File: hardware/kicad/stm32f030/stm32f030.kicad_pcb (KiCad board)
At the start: 2 copper layers, 67.3 x 69.2 mm, 114 parts, among them IC1 AT24CS02-SSHM, K1 RELAY_1RT, K2 RELAY_1RT, P1 5VIN, P10 SWD, P2 LOOP1, P3 LOOP2, P4 RELAY OUT 1, P5 TTL OUT 1, P6 RELAY OUT 2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

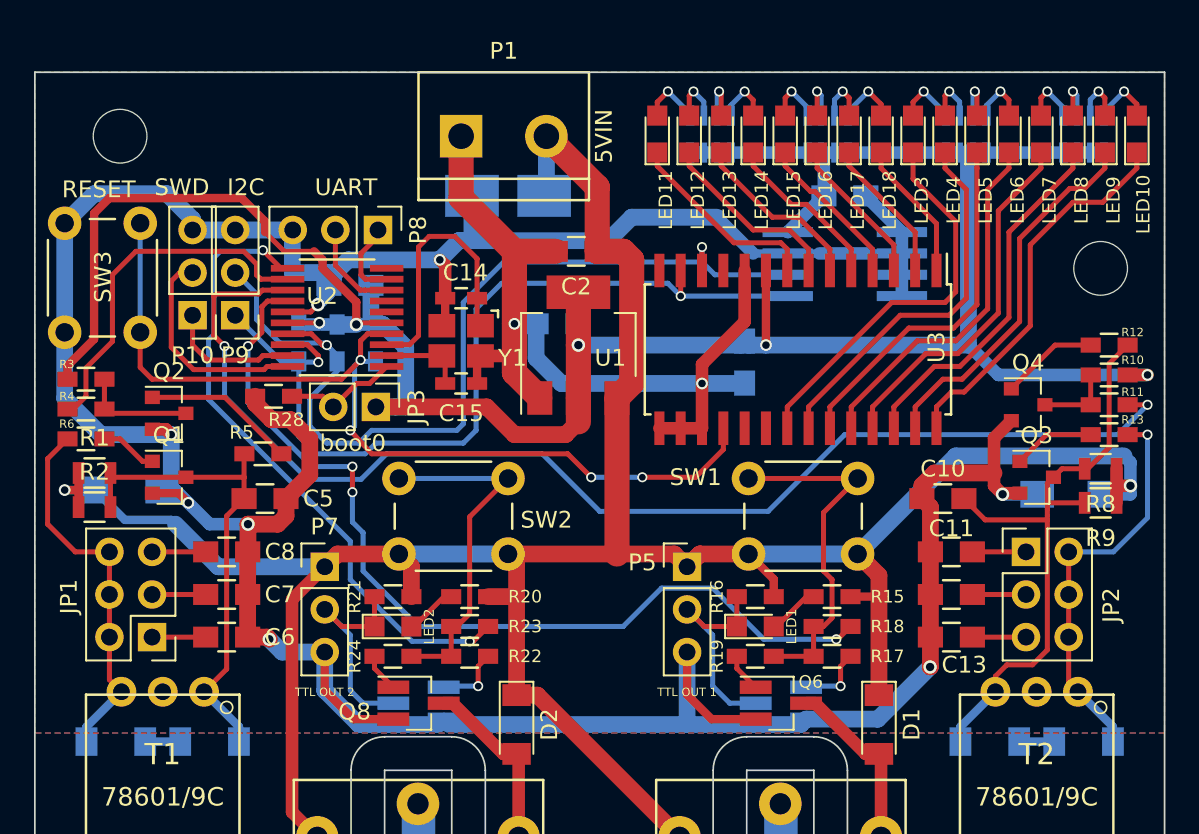
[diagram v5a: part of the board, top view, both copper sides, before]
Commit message: hardware/kicad/stm32f030: use upper layer zones for power
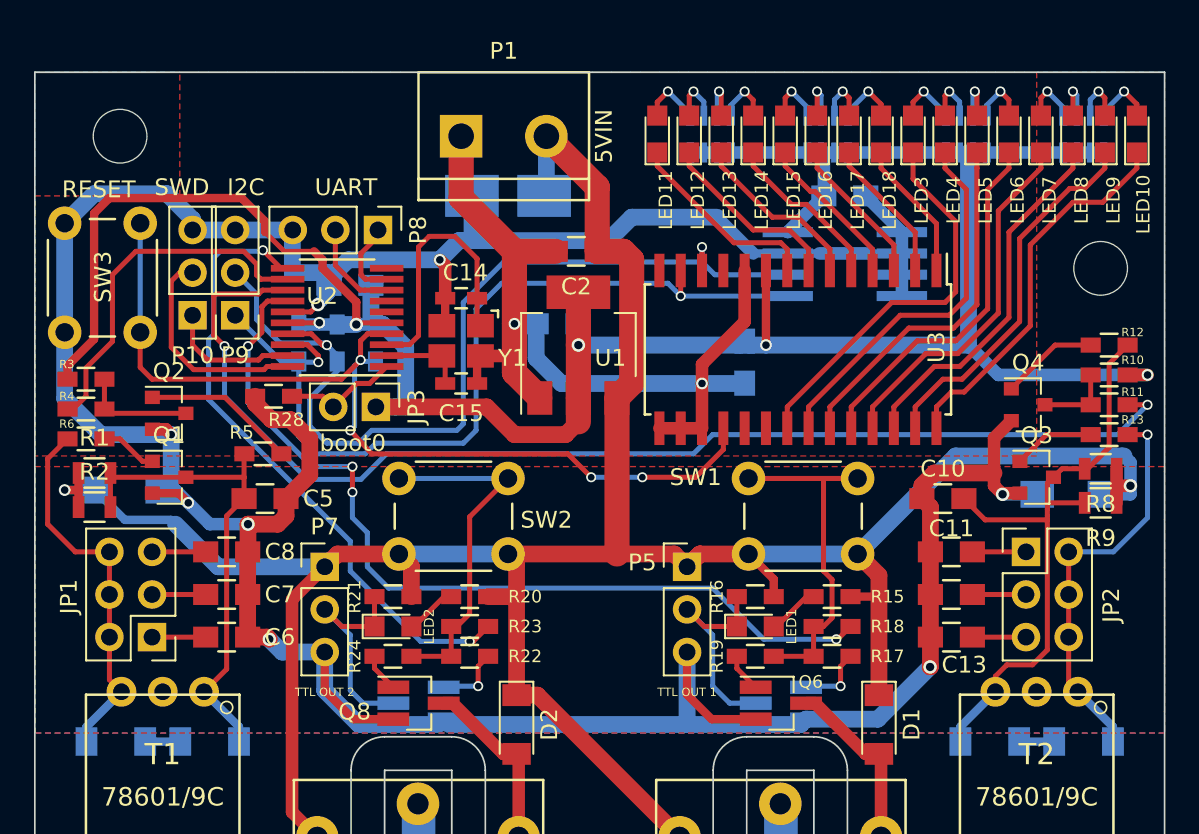
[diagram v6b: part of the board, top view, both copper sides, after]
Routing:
- net /colpitts/osc1: track 73.7 -> 70.8 mm
- net /outputs/active1: track 55.0 -> 52.8 mm
- net Net-(R17-Pad2): track 21.3 -> 20.5 mm
- added copper zone on F.Cu, net +3V3
- added copper zone on F.Cu, net +5V
- removed copper zone on F.Cu, net GND

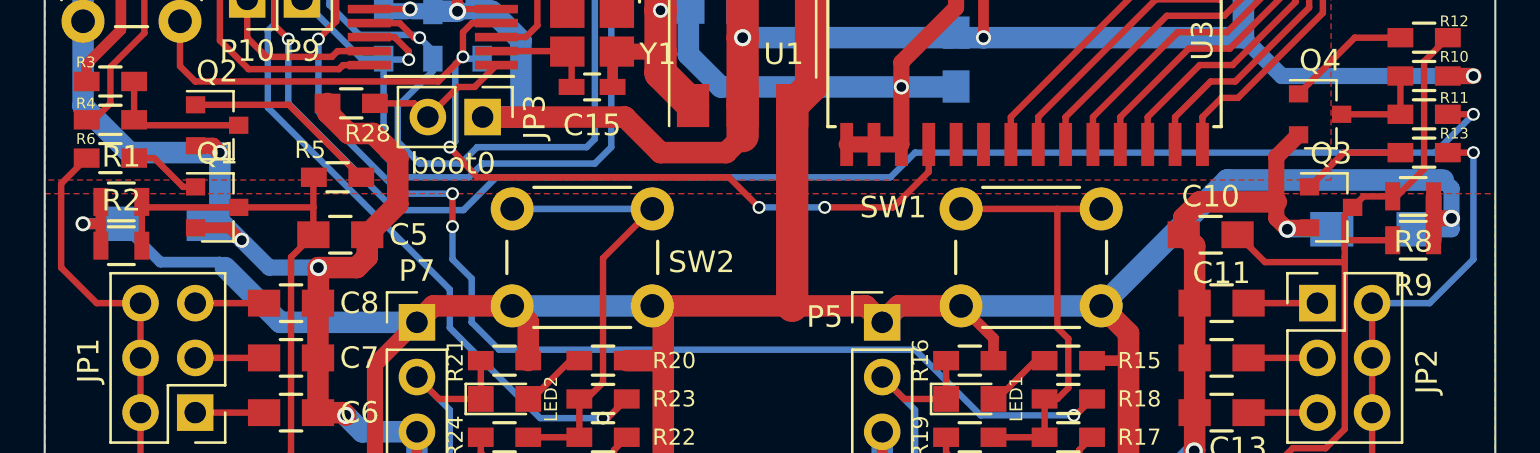
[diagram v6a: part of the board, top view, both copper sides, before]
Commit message: hardware/kicad/stm32f103: MCU/LED block ready
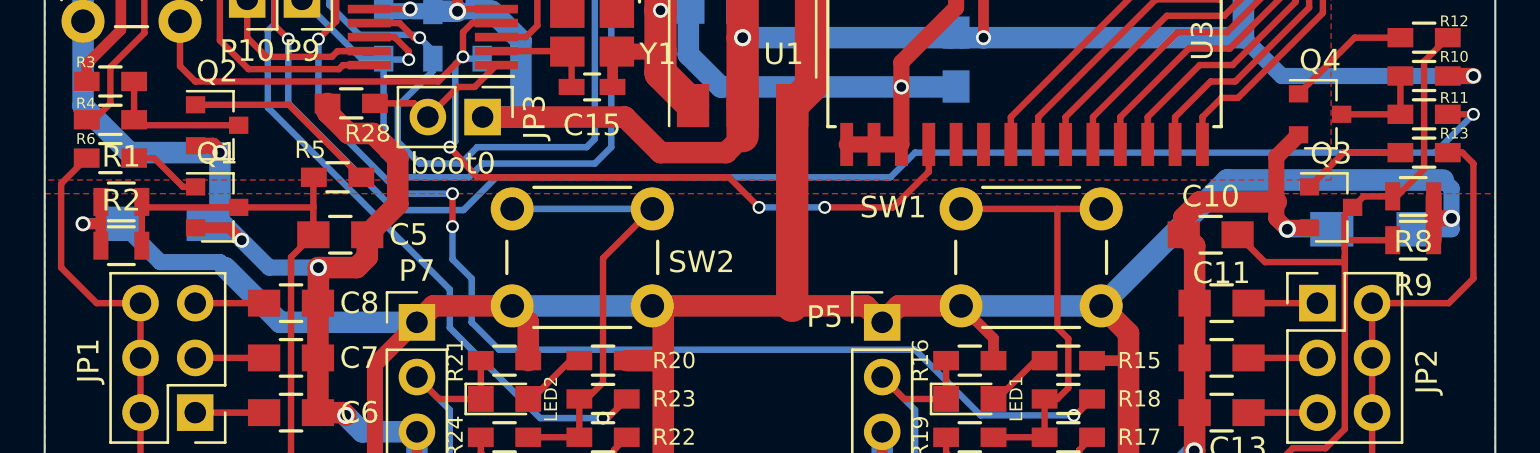
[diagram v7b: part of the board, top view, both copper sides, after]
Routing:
- net Net-(JP2-Pad2): track 24.1 -> 24.3 mm, vias 1 -> 0
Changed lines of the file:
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@@
-(kicad_pcb (version 4) (host pcbnew 4.0.5)
+(kicad_pcb (version 4) (host pcbnew 4.0.5-e0-6337~52~ubuntu16.10.1)
   (general
     (links 243)
@@
     (thickness 1.6)
     (drawings 30)
-    (tracks 823)
+    (tracks 822)
     (zones 0)
     (modules 114)
@@
     (47 F.CrtYd user)
     (48 B.Fab user)
-    (49 F.Fab user)
+    (49 F.Fab user hide)
   )
   (setup
-    (last_trace_width 0.3)
+    (last_trace_width 1)
     (user_trace_width 0.3)
     (user_trace_width 0.4)
@@
   (segment (start 37.338 117.602) (end 39.148 117.602) (width 0.5) (layer B.Cu) (net 1))
   (via (at 37.338 117.602) (size 0.7) (drill 0.45) (layers F.Cu B.Cu) (net 1))
-  (segment (start 43.688 119.38) (end 40.926 119.38) (width 0.5) (layer B.Cu) (net 1))
-  (segment (start 40.926 119.38) (end 39.148 117.602) (width 0.5) (layer B.Cu) (net 1))
+  (segment (start 43.688 119.38) (end 40.926 119.38) (width 0.75) (layer B.Cu) (net 1))
+  (segment (start 40.926 119.38) (end 39.148 117.602) (width 0.75) (layer B.Cu) (net 1))
   (segment (start 46.482 122.174) (end 43.942 119.634) (width 1) (layer B.Cu) (net 1))
   (segment (start 52.832 122.174) (end 46.482 122.174) (width 1) (layer B.Cu) (net 1))
-  (segment (start 43.942 119.634) (end 43.688 119.38) (width 0.5) (layer B.Cu) (net 1))
+  (segment (start 43.942 119.634) (end 43.688 119.38) (width 0.75) (layer B.Cu) (net 1))
   (segment (start 38.894 117.602) (end 39.021 117.729) (width 0.5) (layer B.Cu) (net 1))
   (segment (start 38.166 118.618) (end 38.166 117.602) (width 0.5) (layer F.Cu) (net 1))
@@
   (segment (start 100.838 117.856) (end 100.838 117.348) (width 0.75) (layer B.Cu) (net 1))
   (segment (start 99.282 117.856) (end 100.838 117.856) (width 0.75) (layer B.Cu) (net 1))
-  (segment (start 100.457 115.57) (end 100.33 115.443) (width 0.75) (layer B.Cu) (net 1))
   (segment (start 63.754 121.412) (end 70.245 121.412) (width 1) (layer F.Cu) (net 1))
   (segment (start 64.262 121.92) (end 63.754 121.412) (width 1) (layer F.Cu) (net 1))
@@
   (segment (start 40.005 123.825) (end 40.005 121.285) (width 0.3) (layer F.Cu) (net 20))
   (segment (start 40.005 126.365) (end 40.005 123.825) (width 0.3) (layer F.Cu) (net 20))
-  (segment (start 100.668 114.3) (end 101.854 114.3) (width 0.3) (layer F.Cu) (net 21))
-  (segment (start 99.822 121.285) (end 101.854 119.253) (width 0.3) (layer B.Cu) (net 21))
-  (segment (start 101.854 119.253) (end 101.854 114.3) (width 0.3) (layer B.Cu) (net 21))
-  (via (at 101.854 114.3) (size 0.6) (drill 0.4) (layers F.Cu B.Cu) (net 21))
-  (segment (start 99.822 121.285) (end 97.155 121.285) (width 0.3) (layer B.Cu) (net 21))
+  (segment (start 97.155 121.285) (end 100.711 121.285) (width 0.3) (layer F.Cu) (net 21))
+  (segment (start 101.346 114.3) (end 100.668 114.3) (width 0.3) (layer F.Cu) (net 21))
+  (segment (start 101.854 114.808) (end 101.346 114.3) (width 0.3) (layer F.Cu) (net 21))
+  (segment (start 101.854 120.142) (end 101.854 114.808) (width 0.3) (layer F.Cu) (net 21))
+  (segment (start 100.711 121.285) (end 101.854 120.142) (width 0.3) (layer F.Cu) (net 21))
   (segment (start 99.794 132.588) (end 99.794 131.70656) (width 0.5) (layer B.Cu) (net 21))
   (segment (start 99.794 131.70656) (end 97.70872 129.62128) (width 0.5) (layer B.Cu) (net 21))

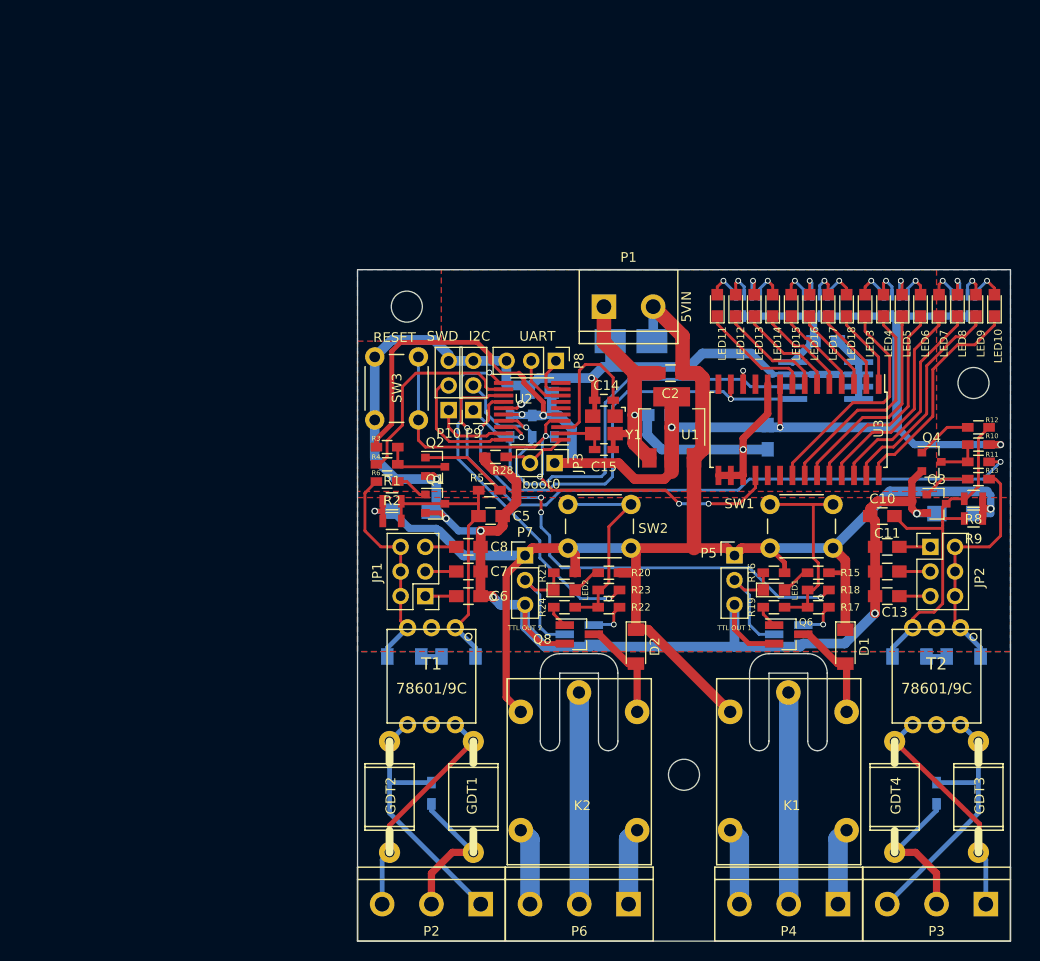
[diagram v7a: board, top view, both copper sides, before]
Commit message: hardware/kicad/stm32f030: Ledbar removed, reorg started
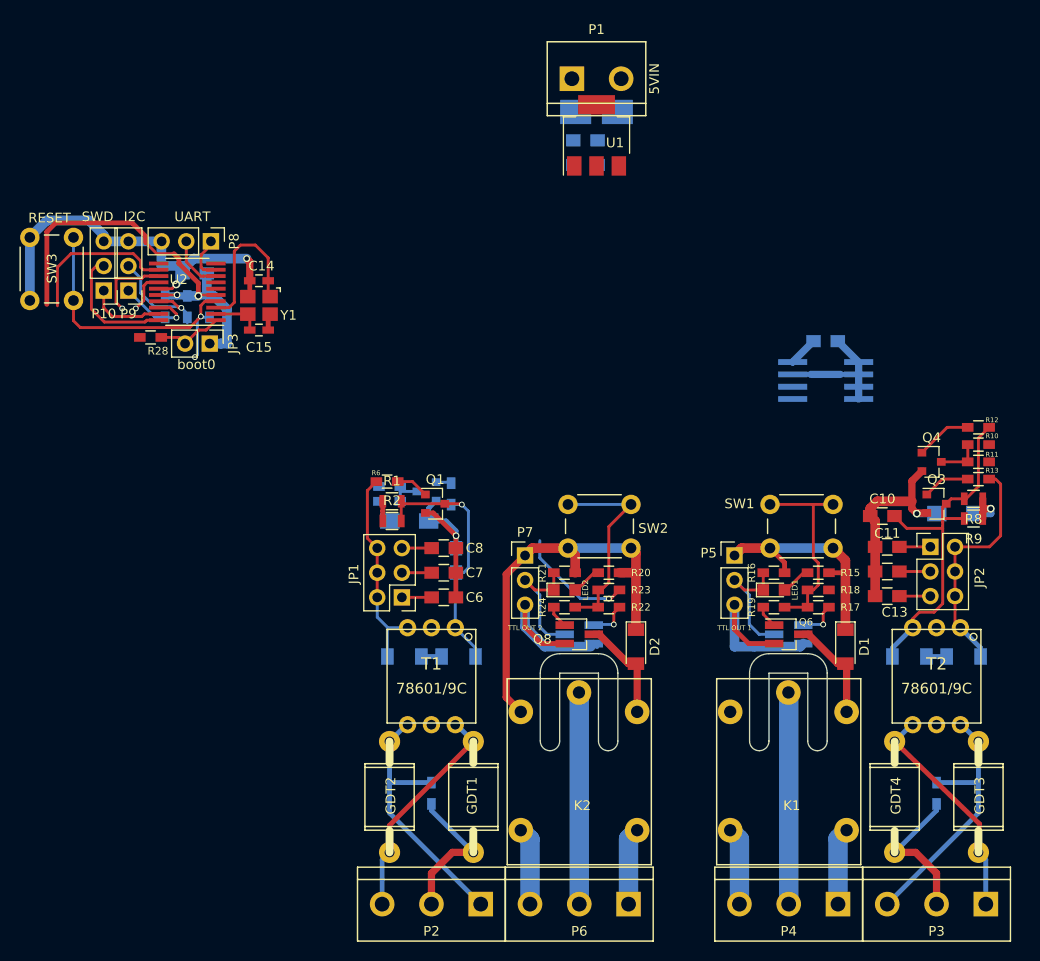
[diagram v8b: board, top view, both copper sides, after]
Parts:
- removed C17: 100n, Capacitors_SMD:C_0805_HandSoldering
- removed LED10, LED11, LED12, LED13, LED14, LED15, LED16, LED17, LED18, LED3, LED4, LED5, LED6, LED7, LED8, LED9: LED_Small, LEDs:LED_0805
- removed REF** (x3): MountingHole_3.2mm_M3, Mounting_Holes:MountingHole_3.2mm_M3
- removed RN1, RN2, RN3, RN4: 220, Resistors_SMD:R_Array_Convex_4x0603_HandSoldering
- removed U3: MCP23017, Housings_SOIC:SOIC-28W_7.5x17.9mm_Pitch1.27mm
- C2, C5, Q2, R3, R4, R5: moved to B.Cu
- moved C14 37.6 mm to (25.4, 93.9)
- moved C15 37.6 mm to (25.4, 98.9)
- moved C16 37.6 mm to (18.8, 93.1)
- moved JP3 37.6 mm to (20.3, 100.3)
- moved P10 37.6 mm to (9.40, 94.9)
- moved P8 37.6 mm to (20.4, 89.8)
- moved R25 37.6 mm to (20.3, 96.5)
- moved R26 37.6 mm to (18.0, 96.5)
- moved R28 37.6 mm to (14.2, 99.7)
- moved SW3 37.6 mm to (1.78, 95.9)
- moved U2 37.6 mm to (18.0, 95.0)
- moved Y1 37.6 mm to (25.4, 96.4)
- moved P9 37.6 mm to (11.9, 94.9)
- moved R27 37.6 mm to (15.7, 96.5)
- moved U1 31.1 mm to (60.2, 78.9)
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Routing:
- net GND: track 272.5 -> 137.0 mm, vias 10 -> 4
- net +3V3: track 155.9 -> 49.8 mm, vias 5 -> 2
- net +5V: track 169.1 -> 74.3 mm, vias 2 -> 1
- net /colpitts/osc1: track 70.8 -> 7.79 mm, vias 2 -> 1
- net /outputs/active1: track 52.8 -> 4.37 mm, vias 4 -> 1
- net /EEPROM/sda: track 53.4 -> 9.10 mm, vias 2 -> 1
- net /EEPROM/scl: track 56.8 -> 12.7 mm, vias 2 -> 1
- net /MCU/reset: track 56.1 -> 30.7 mm, vias 4 -> 2
- net /MCU/active1: track 37.6 -> 12.5 mm, vias 2 -> 1
- net Net-(LED3-Pad1): track 23.5 -> 0.00 mm
- net Net-(LED10-Pad1): track 22.9 -> 0.00 mm
- net Net-(LED4-Pad1): track 22.6 -> 0.00 mm
- net Net-(LED9-Pad1): track 22.3 -> 0.00 mm
- net Net-(LED8-Pad1): track 21.7 -> 0.00 mm
- net Net-(LED7-Pad1): track 21.7 -> 0.00 mm
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- removed copper zone on F.Cu, net +3V3
- removed copper zone on F.Cu, net +5V
- removed copper zone on B.Cu, net GND
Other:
- board size 67.3 x 69.2 mm -> 29.6 x 10 mm
